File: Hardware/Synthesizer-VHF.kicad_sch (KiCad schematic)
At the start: 87 parts, among them J1 Screw_Terminal_01x02, J2 Scope, J3 REF Select, J4 USB-C 2.0 16P, J5 REF_IN, J6 Scope, J7 RFOUTA, J8 Header 1x3, J9 RFOUTB, U1 LM7805A, U2 FT231XQ, U3 ATtiny1616-M, U4 ADF4350, U5 GM1200ACPZ, U6 GM1200ACPZ, X1 IQXO-70

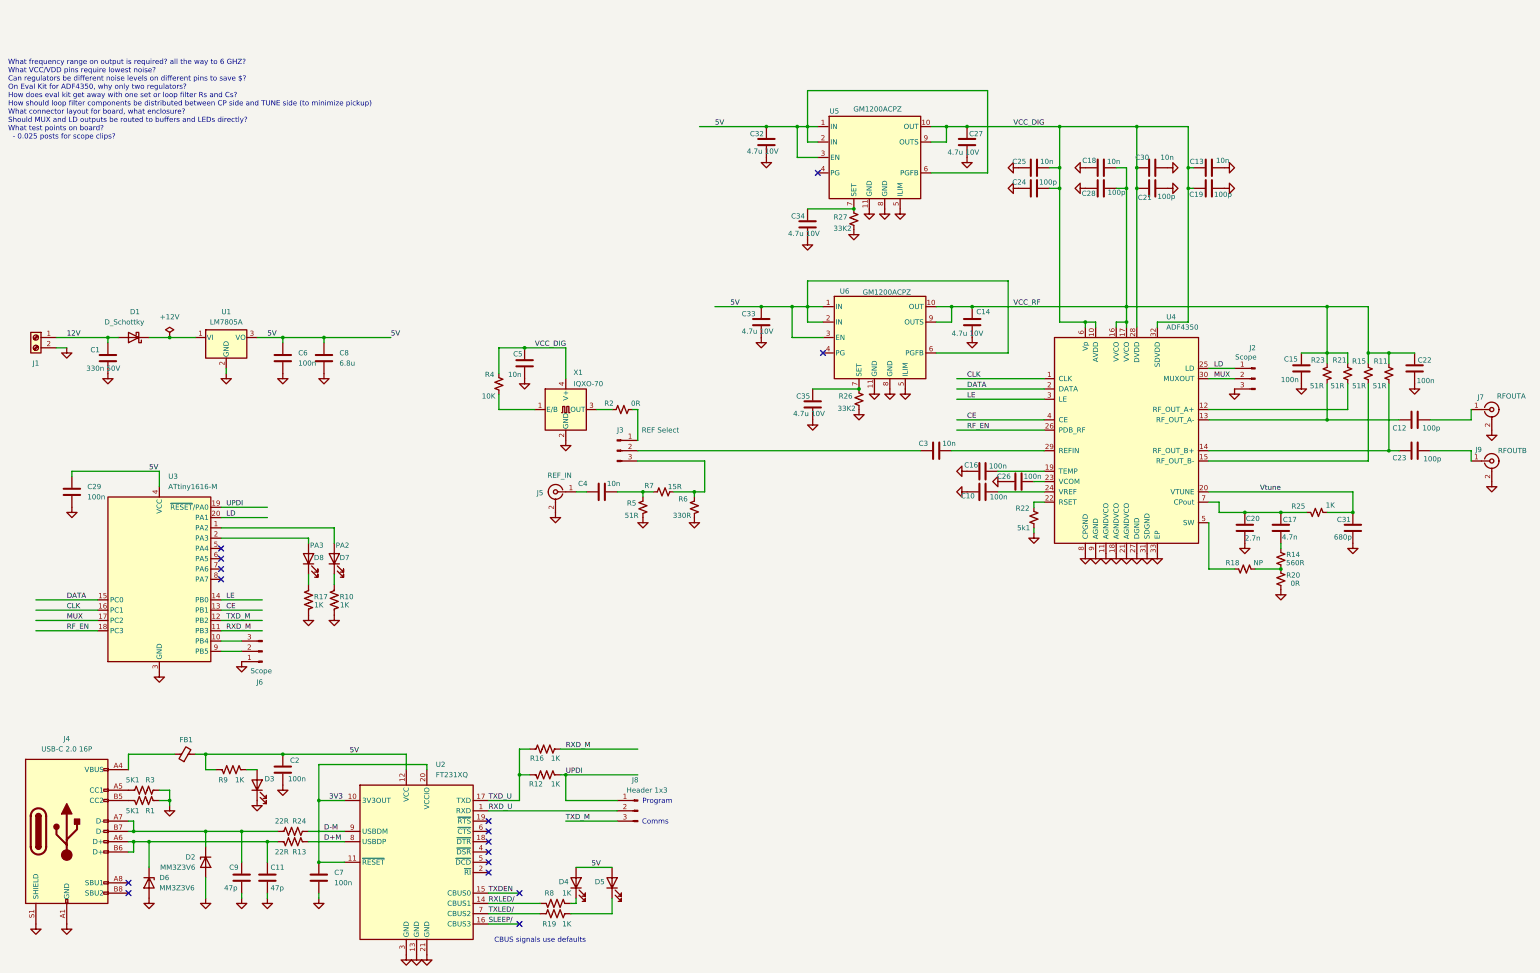
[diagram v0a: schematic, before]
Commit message: Updated layout for 4 layer board as an experiment to check costs Changed low noise regulators to ADP150...used in the Eval board and fancy sig gen example Add more analysis to phase noise spreadsheet, apparently the low V/Hz of the VCO allows cheap regulators
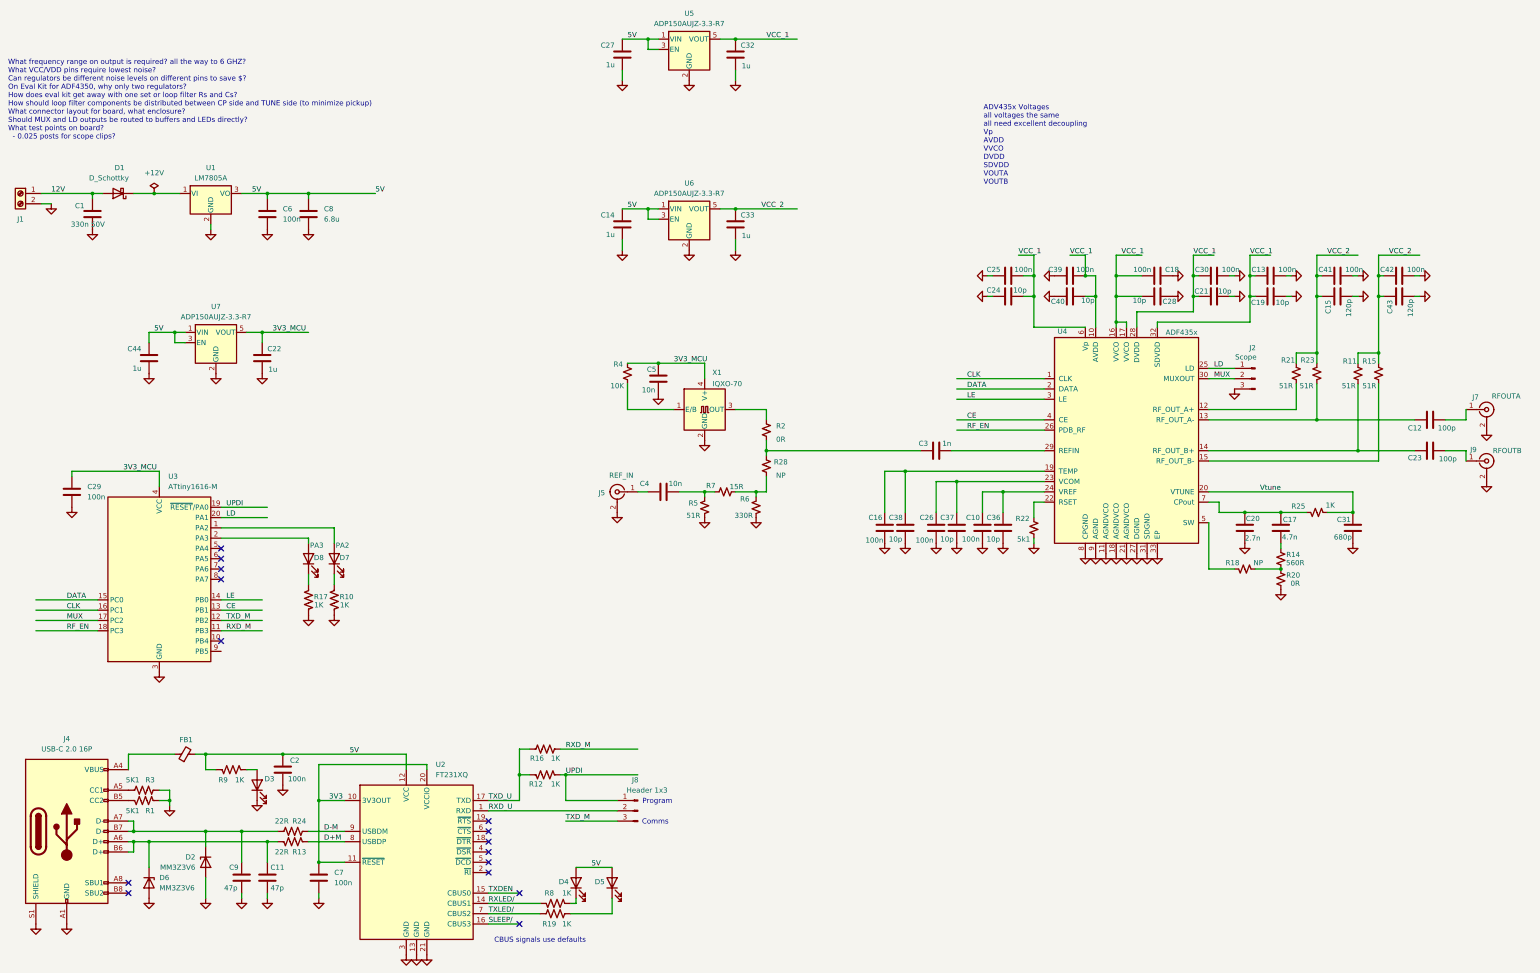
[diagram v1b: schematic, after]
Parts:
- removed C34, C35: 4.7u 10V, Synthesizer:Cap_0402, symbol Device:C
- removed J3: REF Select, Connector_PinHeader_2.54mm:PinHeader_1x03_P2.54mm_Vertical, symbol Connector:Conn_01x03_Pin
- removed J6: Scope, Connector_PinHeader_2.54mm:PinHeader_1x03_P2.54mm_Vertical, symbol Connector:Conn_01x03_Pin
- removed R26, R27: 33K2, Synthesizer:Res_0402, symbol Device:R_Small_US
- removed U5, U6: GM1200ACPZ, Package_DFN_QFN:DFN-10-1EP_3x3mm_P0.5mm_EP1.65x2.38mm_ThermalVias, symbol Synthesizer:GM1200ACPZ
- added C36, C37, C38, C40: 10p, Synthesizer:Cap_0402, symbol Device:C
- added C39, C41, C42: 100n, Synthesizer:Cap_0402, symbol Device:C
- added C43: 120p, Synthesizer:Cap_0402, symbol Device:C
- added C44: 1u, Synthesizer:Cap_0402, symbol Device:C
- added R28: NP, Synthesizer:Res_0402, symbol Device:R_Small_US
- added U5, U6, U7: ADP150AUJZ-3.3-R7, Package_TO_SOT_SMD:SOT-23-5, symbol Synthesizer:ADP150AUJZ-3.3-R7
- C13, C18, C25, C30: value 10n -> 100n
- C14, C27, C33: value 4.7u 10V -> 1u; LCSC C12530 -> C14663
- C15: value 100n -> 120p
- C19, C21, C24, C28: value 100p -> 10p
- C22: value 100n -> 1u; LCSC C15195 -> C14663
- C3: value 10n -> 1n
- C32: value 4.7u 10V -> 1u; LCSC (none) -> C14663
- U4: value ADF4350 -> ADF435x
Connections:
- net 5V: now also C14.1, C27.1, C44.1, U5.1 (VIN), U5.3 (EN), U6.1 (VIN), U6.3 (EN), U7.1 (VIN), U7.3 (EN); no longer C29.1, C32.1, C33.1, U3.4 (VCC)
- net GND: now also C36.1, C37.1, C38.1, C39.2, C40.1, C41.2, C42.2, C43.2, C44.2, U5.2 (GND), U6.2 (GND), U7.2 (GND)
- net at X1.3 (OUT): now also R2.2; no longer R2.1
- net at R6.1, R7.2: now also R28.1
- net at C16.2, U4.19 (TEMP): now also C38.2
- net at C26.1, U4.23 (VCOM): now also C37.2
- net at C10.1, U4.24 (VREF): now also C36.2
- net at C3.2: now also R2.1, R28.2
- net VCC_DIG renamed VCC_1
- net VCC_1: now also C18.1, C28.2, C32.1, U4.16 (VVCO), U4.17 (VVCO), C39.1, C40.2, U5.5 (VOUT); no longer C27.1, C5.2, R4.2, X1.4 (V+)
- removed net VCC_RF: C14.1, C15.1, C18.1, C22.1, C28.2, R11.2, R15.2, R21.2, R23.2, U4.16 (VVCO), U4.17 (VVCO)
- new net 3V3_MCU: C22.1, C29.1, C5.2, R4.2, U3.4 (VCC), U7.5 (VOUT), X1.4 (V+)
- new net VCC_2: C15.1, C33.1, C41.1, C42.1, C43.1, R11.2, R15.2, R21.2, R23.2, U6.5 (VOUT)
- no-connect marks 16 -> 15
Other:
- note added: "ADV435x Voltages all voltages the same all need excellent decoupling Vp AVDD VVCO DVDD SDVDD VOUTA VOUTB"
- moved on the sheet: C1, C10, C12, C13, C15, C16, C18, C19, C21, C23, C24, C25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

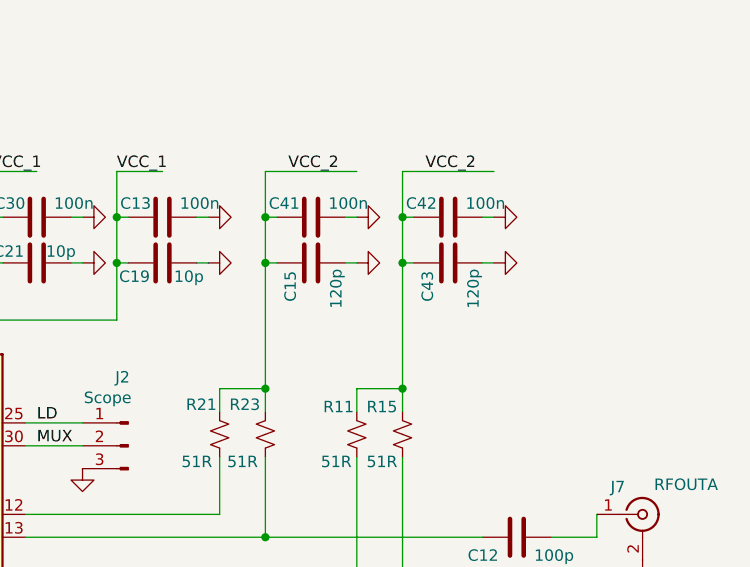
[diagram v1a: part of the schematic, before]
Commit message: final commit for 4 layer with parts on back side...that add a lot of cost Design uses a single supply with massive decoupling because EVKIT and Hellmich sig gen did it that way.  Also parts on back side may not improve grounding because of pwr via to get to cap.
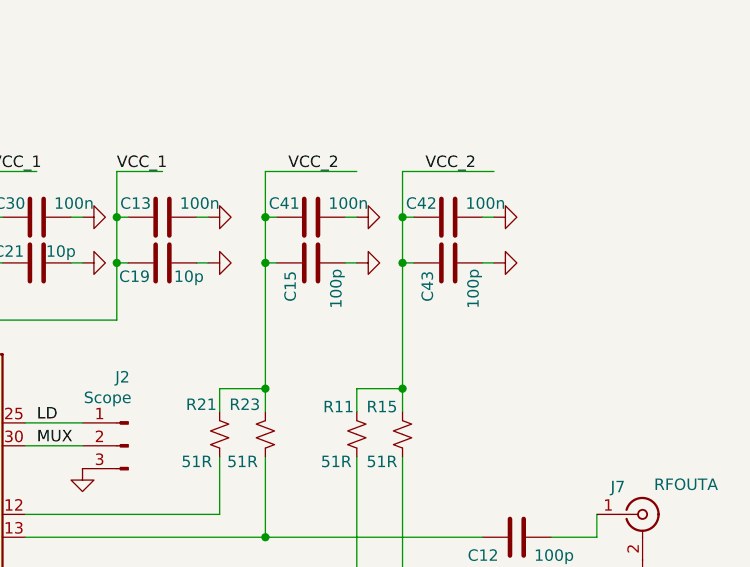
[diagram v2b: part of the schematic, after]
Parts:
- C15, C43: value 120p -> 100p
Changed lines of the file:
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@@
 			)
 		)
-		(property "Value" "120p"
+		(property "Value" "100p"
 			(at 345.694 100.33 0)
 			(effects
@@
 			)
 		)
-		(property "Value" "120p"
+		(property "Value" "100p"
 			(at 360.934 100.33 0)
 			(effects
